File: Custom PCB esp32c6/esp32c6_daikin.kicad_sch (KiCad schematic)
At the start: 31 parts, among them J2 Conn_01x07, Q1 BSS138PS, U1 TPS562246, U2 WT0132C6-S5

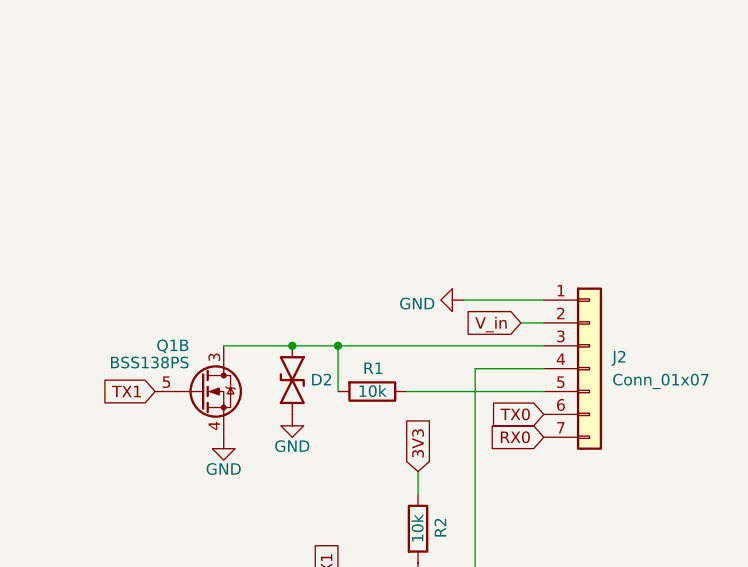
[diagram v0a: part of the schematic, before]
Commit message: fix(sch): add 12V input PTC + TVS and S21 series resistors
TPS562246 is 17V-rec/19V-abs-max on a 12-14V rail with no clamp; SMF15A
clamps hot-plug ring near breakdown, under abs-max. PTC protects the
aircon supply. 220R series resistors cap fault current into the level
shift, per faikin32 baseline BOM.
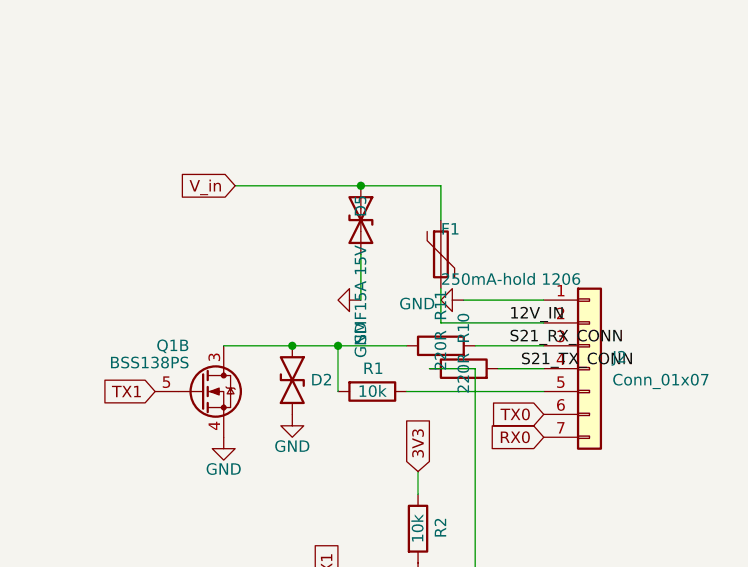
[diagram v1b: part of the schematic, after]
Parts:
- added D5: SMF15A 15V, symbol Device:D_TVS
- added F1: 250mA-hold 1206, symbol Device:Polyfuse
- added R10, R11: 220R, symbol Device:R
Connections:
- net GND: now also D5.2 (A2)
- net V_in: now also D5.1 (A1), F1.1; no longer J2.2 (Pin_2)
- net at D3.2, D4.1 (K), Q1.2 (GN): now also R10.1; no longer J2.4 (Pin_4)
- net at D2.2, Q1.3 (SP), R1.2: now also R11.1; no longer J2.3 (Pin_3)
- new net 12V_IN: F1.2, J2.2 (Pin_2)
- new net S21_RX_CONN: J2.3 (Pin_3), R11.2
- new net S21_TX_CONN: J2.4 (Pin_4), R10.2

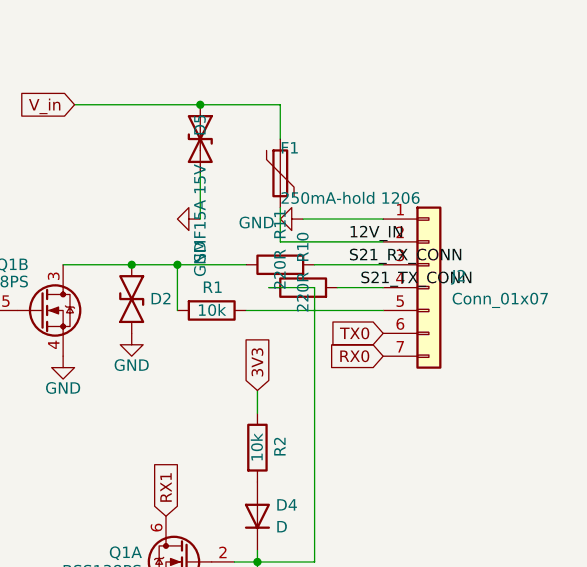
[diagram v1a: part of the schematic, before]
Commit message: feat(sch): S21-standard keyed JST-EH connector
Replaces the non-keyed 7-pin 0.1in header. Standard Daikin BRP069B41
lead mates directly; keying provides the reverse-mate protection.
Debug UART pins dropped; module USB covers debug.
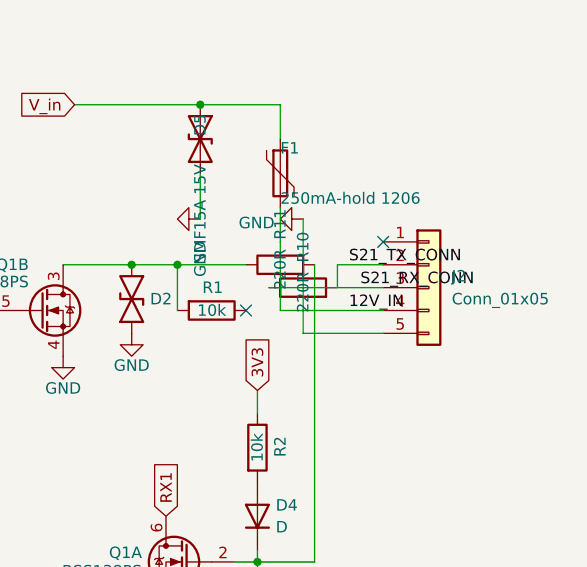
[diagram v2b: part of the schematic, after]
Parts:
- J2: value Conn_01x07 -> Conn_01x05; footprint Connector_PinHeader_2.54mm:PinHeader_1x07_P2.54mm_Horizontal -> Connector_JST:JST_EH_S5B-EH_1x05_P2.50mm_Horizontal; symbol Connector_Generic:Conn_01x07 -> Connector_Generic:Conn_01x05
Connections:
- net 12V_IN: now also J2.4 (Pin_4); no longer J2.2 (Pin_2)
- net GND: now also J2.5 (Pin_5); no longer J2.1 (Pin_1)
- net RX0: no longer J2.7 (Pin_7)
- net S21_RX_CONN: now also D3.2, D4.1 (K), Q1.2 (GN), R10.1
- net S21_TX_CONN: now also J2.2 (Pin_2); no longer J2.4 (Pin_4)
- net TX0: no longer J2.6 (Pin_6)
- net at R1.1: no longer J2.5 (Pin_5)
- no-connect marks 0 -> 2
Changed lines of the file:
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@@
 	(wire
 		(pts
-			(xy 215.9 73.66) (xy 224.79 73.66)
+			(xy 215.9 73.66) (xy 215.9 86.36)
+		)
+		(stroke
+			(width 0)
+			(type default)
+		)
+	)
+	(wire
+		(pts
+			(xy 215.9 86.36) (xy 224.79 86.36)
 		)
 		(stroke
@@
 		)
 	)
-	(wire
-		(pts
-			(xy 209.55 83.82) (xy 224.79 83.82)
-		)
-		(stroke
-			(width 0)
-			(type default)
-		)
+	(no_connect
+		(at 209.55 83.82)
 	)
 	(wire
@@
 	(wire
 		(pts
-			(xy 224.79 76.2) (xy 213.36 76.2)
-		)
-		(stroke
-			(width 0)
-			(type default)
-		)
+			(xy 213.36 76.2) (xy 213.36 83.82)
+		)
+		(stroke
+			(width 0)
+			(type default)
+		)
+	)
+	(wire
+		(pts
+			(xy 213.36 83.82) (xy 224.79 83.82)
+		)
+		(stroke
+			(width 0)
+			(type default)
+		)
+	)
+	(no_connect
+		(at 224.79 76.2)
 	)
 	(wire
@@
 	(wire
 		(pts
-			(xy 219.71 81.28) (xy 224.79 81.28)
+			(xy 219.71 81.28) (xy 219.71 78.74)
+		)
+		(stroke
+			(width 0)
+			(type default)
+		)
+	)
+	(wire
+		(pts
+			(xy 219.71 78.74) (xy 224.79 78.74)
 		)
 		(stroke
@@
 	(wire
 		(pts
-			(xy 217.17 78.74) (xy 224.79 78.74)
+			(xy 217.17 78.74) (xy 217.17 81.28)
+		)
+		(stroke
+			(width 0)
+			(type default)
+		)
+	)
+	(wire
+		(pts
+			(xy 217.17 81.28) (xy 224.79 81.28)
 		)
 		(stroke
@@
 	)
 	(label "12V_IN"
-		(at 220.98 76.2 0)
+		(at 220.98 83.82 0)
 		(effects
 			(font
@@
 	)
 	(label "S21_TX_CONN"
-		(at 222.25 81.28 0)
+		(at 220.98 78.74 0)
 		(effects
 			(font
@@
 	)
 	(label "S21_RX_CONN"
-		(at 220.98 78.74 0)
+		(at 222.25 81.28 0)
 		(effects
 			(font
@@
 		)
 	)
-	(global_label "TX0"
-		(shape input)
-		(at 224.79 86.36 180)
-		(fields_autoplaced yes)
-		(effects
-			(font
-				(size 1.27 1.27)
-			)
-			(justify right)
-		)
-		(property "Intersheetrefs" "${INTERSHEET_REFS}"
-			(at 218.4182 86.36 0)
-			(hide yes)
-			(show_name no)
-			(do_not_autoplace no)
-			(effects
-				(font
-					(size 1.27 1.27)
-				)
-				(justify right)
-			)
-		)
-	)
 	(global_label "3V3"
 		(shape input)
@@
 				)
 				(justify left)
-			)
-		)
-	)
-	(global_label "RX0"
-		(shape input)
-		(at 224.79 88.9 180)
-		(fields_autoplaced yes)
-		(effects
-			(font
-				(size 1.27 1.27)
-			)
-			(justify right)
-		)
-		(property "Intersheetrefs" "${INTERSHEET_REFS}"
-			(at 218.1158 88.9 0)
-			(hide yes)
-			(show_name no)
-			(do_not_autoplace no)
-			(effects
-				(font
-					(size 1.27 1.27)
-				)
-				(justify right)
 			)
 		)
@@
 	)
 	(symbol
-		(lib_id "Connector_Generic:Conn_01x07")
+		(lib_id "Connector_Generic:Conn_01x05")
 		(at 229.87 81.28 0)
 		(unit 1)
@@
 			)
 		)
-		(property "Value" "Conn_01x07"
+		(property "Value" "Conn_01x05"
 			(at 232.41 82.5499 0)
 			(show_name no)
@@
 			)
 		)
-		(property "Footprint" "Connector_PinHeader_2.54mm:PinHeader_1x07_P2.54mm_Horizontal"
+		(property "Footprint" "Connector_JST:JST_EH_S5B-EH_1x05_P2.50mm_Horizontal"
 			(at 229.87 81.28 0)
 			(hide yes)
@@
 			)
 		)
-		(property "Description" "Generic connector, single row, 01x07, script generated (kicad-library-utils/schlib/autogen/connector/)"
+		(property "Description" "Generic connector, single row, 01x05, script generated (kicad-library-utils/schlib/autogen/connector/)"
 			(at 229.87 81.28 0)
 			(hide yes)
@@
 		(pin "5"
 		)
-		(pin "6"
-		)
-		(pin "7"
-		)
 		(instances

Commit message: fix(bom): LCSC part numbers for all placeable parts
U2 and J2 shipped blank and would arrive unplaced from JLC assembly.
New protection parts included. BOM_rev-b.csv is the assembly BOM.
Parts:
- D2, D3: LCSC (none) -> C5137770
- D4: LCSC (none) -> C28642302
- D5: footprint (none) -> Diode_SMD:D_SOD-123F; LCSC (none) -> C123802
- F1: footprint (none) -> Fuse:Fuse_1206_3216Metric; LCSC (none) -> C99561
- J2: LCSC (none) -> C265103
- Q1: LCSC (none) -> C193381
- R1, R2: LCSC (none) -> C25744
- R10, R11: footprint (none) -> Resistor_SMD:R_0603_1608Metric; LCSC (none) -> C1226
- U2: LCSC (none) -> C9900241604
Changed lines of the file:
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@@
 			)
 		)
+		(property "LCSC" "C5137770"
+			(at 210.82 116.205 0)
+			(hide yes)
+			(show_name no)
+			(do_not_autoplace no)
+			(effects
+				(font
+					(size 1.27 1.27)
+				)
+			)
+		)
 		(pin "2"
 		)
@@
 			)
 		)
+		(property "LCSC" "C193381"
+			(at 186.69 83.82 0)
+			(hide yes)
+			(show_name no)
+			(do_not_autoplace no)
+			(effects
+				(font
+					(size 1.27 1.27)
+				)
+			)
+		)
 		(pin "1"
 		)
@@
 			)
 		)
+		(property "LCSC" "C9900241604"
+			(at 88.9 111.76 0)
+			(hide yes)
+			(show_name no)
+			(do_not_autoplace no)
+			(effects
+				(font
+					(size 1.27 1.27)
+				)
+			)
+		)
 		(pin "5"
 		)
@@
 			)
 		)
+		(property "LCSC" "C265103"
+			(at 229.87 81.28 0)
+			(hide yes)
+			(show_name no)
+			(do_not_autoplace no)
+			(effects
+				(font
+					(size 1.27 1.27)
+				)
+			)
+		)
 		(pin "1"
 		)
@@
 			)
 		)
+		(property "LCSC" "C5137770"
+			(at 196.85 82.55 0)
+			(hide yes)
+			(show_name no)
+			(do_not_autoplace no)
+			(effects
+				(font
+					(size 1.27 1.27)
+				)
+			)
+		)
 		(pin "2"
 		)
@@
 			)
 		)
+		(property "LCSC" "C193381"
+			(at 203.2 111.76 0)
+			(hide yes)
+			(show_name no)
+			(do_not_autoplace no)
+			(effects
+				(font
+					(size 1.27 1.27)
+				)
+			)
+		)
 		(pin "1"
 		)
@@
 			)
 		)
+		(property "LCSC" "C28642302"
+			(at 210.82 106.68 0)
+			(hide yes)
+			(show_name no)
+			(do_not_autoplace no)
+			(effects
+				(font
+					(size 1.27 1.27)
+				)
+			)
+		)
 		(pin "1"
 		)
@@
 			)
 		)
+		(property "LCSC" "C25744"
+			(at 205.74 83.82 0)
+			(hide yes)
+			(show_name no)
+			(do_not_autoplace no)
+			(effects
+				(font
+					(size 1.27 1.27)
+				)
+			)
+		)
 		(pin "1"
 		)
@@
 			)
 		)
+		(property "LCSC" "C25744"
+			(at 210.82 99.06 0)
+			(hide yes)
+			(show_name no)
+			(do_not_autoplace no)
+			(effects
+				(font
+					(size 1.27 1.27)
+				)
+			)
+		)
 		(pin "1"
 		)
@@
 			)
 		)
-		(property "Footprint" ""
+		(property "Footprint" "Fuse:Fuse_1206_3216Metric"
 			(at 213.36 68.58 0)
 			(hide yes)
@@
 			)
 		)
+		(property "LCSC" "C99561"
+			(at 213.36 68.58 0)
+			(hide yes)
+			(show_name no)
+			(do_not_autoplace no)
+			(effects
+				(font
+					(size 1.27 1.27)
+				)
+			)
+		)
 		(pin "1"
 		)
@@
 			)
 		)
-		(property "Footprint" ""
+		(property "Footprint" "Diode_SMD:D_SOD-123F"
 			(at 204.47 64.77 0)
 			(hide yes)
@@
 			)
 		)
+		(property "LCSC" "C123802"
+			(at 204.47 64.77 0)
+			(hide yes)
+			(show_name no)
+			(do_not_autoplace no)
+			(effects
+				(font
+					(size 1.27 1.27)
+				)
+			)
+		)
 		(pin "1"
 		)
@@
 			)
 		)
-		(property "Footprint" ""
+		(property "Footprint" "Resistor_SMD:R_0603_1608Metric"
 			(at 215.9 81.28 0)
 			(hide yes)
@@
 			)
 		)
+		(property "LCSC" "C1226"
+			(at 215.9 81.28 0)
+			(hide yes)
+			(show_name no)
+			(do_not_autoplace no)
+			(effects
+				(font
+					(size 1.27 1.27)
+				)
+			)
+		)
 		(pin "1"
 		)
@@
 			)
 		)
-		(property "Footprint" ""
+		(property "Footprint" "Resistor_SMD:R_0603_1608Metric"
 			(at 213.36 78.74 0)
 			(hide yes)
@@
 			(at 213.36 78.74 0)
 			(hide yes)
+			(show_name no)
+			(do_not_autoplace no)
+			(effects
+				(font
+					(size 1.27 1.27)
+				)
+			)
+		)
+		(property "LCSC" "C1226"
+			(at 213.36 78.74 0)
+			(hide yes)

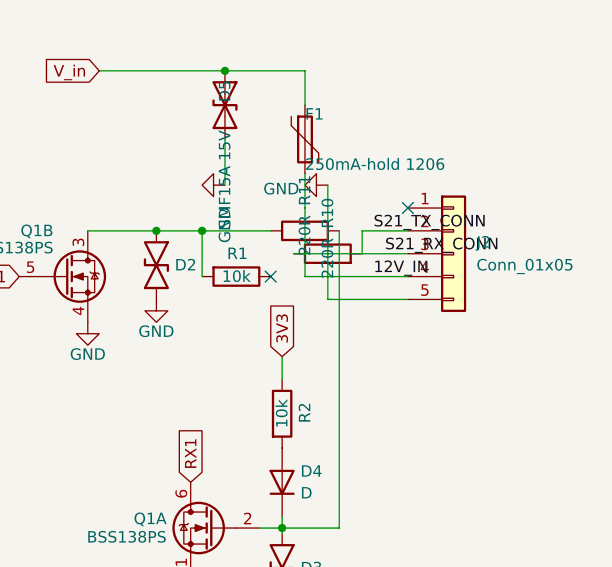
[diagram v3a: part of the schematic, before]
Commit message: fix(sch+pcb): separate the two S21 signal nets merged by the JST-EH swap
The Task-6 JST-EH connector swap merged two S21 nets into one, tying
J2 pin 2 (aircon Tx) and J2 pin 3 (aircon Rx) together through R10 (220R)
and feeding the ESP's TX back into its RX front end. A single wire carrying
the /S21_RX_CONN label at the R10.1 row shorted J2.3, R11.2, and the
Q1.2/D3/D4 gate cluster onto one 6-node net.

This restores the Task-5 (commit 2981aef) two-net split, adapted to the new
JST-EH pin numbers:
  - /S21_TX_CORE (new label; was Net-(D4-K)) = {R10.1, Q1.2, D3.2, D4.1}
  - /S21_RX_CONN (reduced to)                = {J2.3, R11.2}
J2.2 and J2.3 now share no path except through the intended full front end.

Schematic: split the merge wire into two electrically separate wires and
added the S21_TX_CORE label; the four nets are netlist-verified (kicad-cli
export) with exactly the target node sets. ERC unchanged at 16 errors.

PCB: created net /S21_TX_CORE, reassigned pads R10.1/Q1.2/D3.2/D4.1 and
their cluster copper to it, deleted the two bridge tracks (R11.2->R10.1
vertical on F.Cu and J2.3->hub on B.Cu), and routed a new R11.2->J2.3 RX
path (F.Cu stub + via + B.Cu run under the 12V/TX columns). DRC clean:
0 unconnected, 0 errors, 0 schematic-parity mismatches, 1 zone.

refill.py: corrected the wx assert-suppression guard order (DisableAsserts
after importing pcbnew, with a wx.App) so refills no longer raise dialogs.
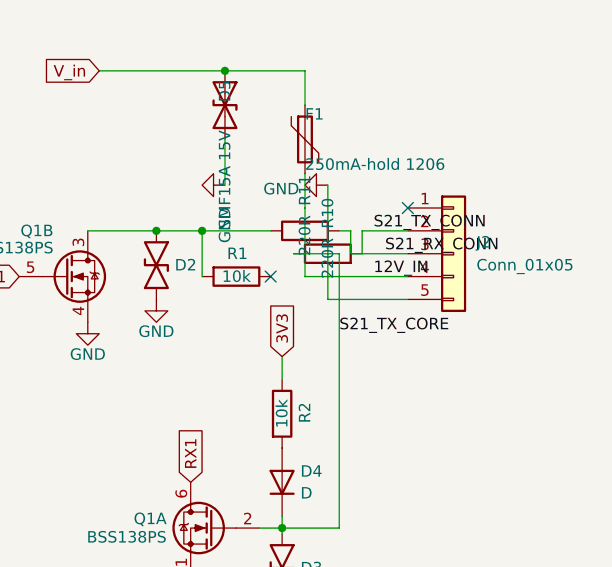
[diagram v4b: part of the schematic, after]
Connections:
- net S21_RX_CONN: no longer D3.2, D4.1 (K), Q1.2 (GN), R10.1
- new net S21_TX_CORE: D3.2, D4.1 (K), Q1.2 (GN), R10.1
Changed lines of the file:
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@@
 	(wire
 		(pts
-			(xy 217.17 78.74) (xy 217.17 81.28)
+			(xy 217.17 78.74) (xy 218.44 78.74)
 		)
 		(stroke
@@
 	(wire
 		(pts
-			(xy 217.17 81.28) (xy 224.79 81.28)
+			(xy 218.44 81.28) (xy 224.79 81.28)
 		)
 		(stroke
@@
 		(effects
 			(font
+				(size 1.27 1.27)
+			)
+			(justify left bottom)
+		)
+	)
+	(wire
+		(pts
+			(xy 218.44 78.74) (xy 218.44 81.28)
+		)
+		(stroke
+			(width 0)
+			(type default)
+		)
+	)
+	(label "S21_TX_CORE"
+		(at 217.17 90.17 0)
+		(effects
+			(font

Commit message: feat(xiao-sch): delete WT0132C6 module + button circuitry
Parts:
- removed Boot1, Matter1, Reset1: Tactile Button, 160gf, easyeda2kicad:SW-SMD_L3.9-W3.0-P4.45, symbol JLCPCB-Connectors_Buttons:Tactile Button, 160gf, 12V, 50mA, 4.0mm
- removed C1, C2, C4, C5, C7, C8: 100nF, easyeda2kicad:C0402, symbol Device:C
- removed C6: 1uF, easyeda2kicad:C0603, symbol Device:C
- removed D4: D, easyeda2kicad:D0402, symbol Device:D
- removed R9: 220, easyeda2kicad:R0402, symbol Device:R
- removed U2: WT0132C6-S5, easyeda2kicad:WT0132C6-S5, symbol easyeda2kicad:WT0132C6-S5

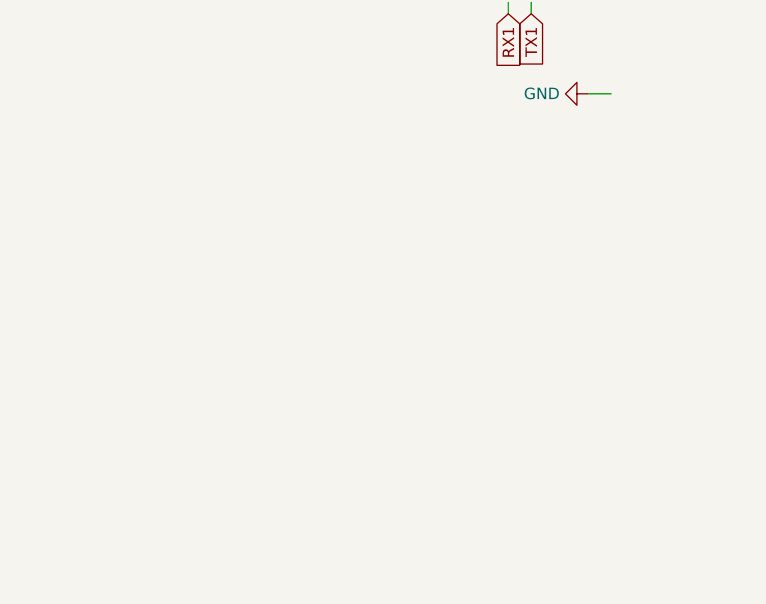
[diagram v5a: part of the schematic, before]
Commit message: feat(xiao-sch): add XIAO ESP32-C6 symbol + both-capable footprint
Add U2 = Seeed XIAO ESP32-C6, reusing the reference designator freed
by the Task 2 module deletion. Not wired yet (Tasks 4/5 wire UART and
power); pins left ready.

Source: official Seeed OPL KiCad library (Seeed-Studio/OPL_Kicad_Library,
"Seeed Studio XIAO Series Library"). Symbol XIAO-ESP32-C6-SMD (24 pins)
and footprint XIAO-ESP32-C6-DIP copied verbatim into a project-local lib
(lib/Seeed_Studio_XIAO_Series.kicad_sym, lib/Seeed_XIAO.pretty) with new
sym-lib-table / fp-lib-table.

Footprint is both-capable by construction: each of the 14 main edge pads
has BOTH a plated through-hole (header/socket mount) and an outward SMD
edge pad (direct edge-reflow). 2 rows of 7, 2.54mm pitch, 15.24mm
row-to-row spacing per the Seeed mechanical drawing. Default footprint
of the project symbol set to the DIP (both-capable) variant.

Named pads verified against the official pinout: D6=pad7 (GPIO16/TX),
D7=pad8 (GPIO17/RX), 3V3_OUT=pad12, GND=pad13, VBUS=pad14 (5V pad).
Symbol pins 1-14 map 1:1 to footprint pads 1-14. Symbol pins 15-24 are
the module's optional bottom debug (JTAG/EN/BOOT) and battery (VBAT/GND)
pads, all passive and unused here; a DIP/header land pattern cannot land
them (not on the edge), so they are intentionally unconnected.

Verify: netlist exports clean, U2 present; ERC delta vs Task 2 is only
+24 pin_not_connected (U2's unwired pins), no other new violations.
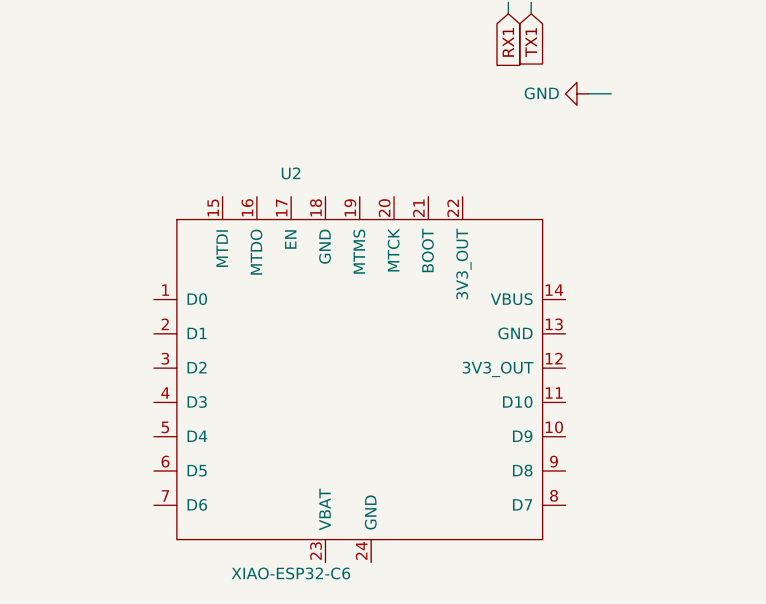
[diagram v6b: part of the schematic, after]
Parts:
- added U2: XIAO-ESP32-C6, Seeed_XIAO:XIAO-ESP32-C6-DIP, symbol Seeed_Studio_XIAO_Series:XIAO-ESP32-C6-SMD
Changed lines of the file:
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@@
+		)
+	)
+	(symbol
+		(lib_id "Seeed_Studio_XIAO_Series:XIAO-ESP32-C6-SMD")
+		(at 63.5 170.18 0)
+		(unit 1)
+		(body_style 1)
+		(exclude_from_sim no)
+		(in_bom yes)
+		(on_board yes)
+		(in_pos_files yes)
+		(dnp no)
+		(property "Reference" "U2"
+			(at 63.5 148.59 0)
+			(effects
+				(font
+					(size 1.27 1.27)
+				)
+			)
+		)
+		(property "Value" "XIAO-ESP32-C6"
+			(at 63.5 193.04 0)
+			(effects
+				(font
+					(size 1.27 1.27)
+				)
+			)
+		)
+		(property "Footprint" "Seeed_XIAO:XIAO-ESP32-C6-DIP"
+			(at 63.5 170.18 0)
+			(hide yes)
+			(effects
+				(font
+					(size 1.27 1.27)
+				)
+			)
+		)
+		(property "Datasheet" "https://wiki.seeedstudio.com/xiao_esp32c6_getting_started/"
+			(at 63.5 170.18 0)
+			(hide yes)
+			(effects
+				(font
+					(size 1.27 1.27)
+				)
+			)
+		)
+		(property "Description" "Seeed Studio XIAO ESP32-C6"
+			(at 63.5 170.18 0)
+			(hide yes)
+			(effects
+				(font
+					(size 1.27 1.27)
+				)
+			)
+		)
+		(pin "1"
+		)
+		(pin "2"
+		)
+		(pin "3"
+		)
+		(pin "4"
+		)
+		(pin "5"
+		)
+		(pin "6"
+		)
+		(pin "7"
+		)
+		(pin "8"
+		)
+		(pin "9"
+		)
+		(pin "10"
+		)
+		(pin "11"
+		)
+		(pin "12"
+		)
+		(pin "13"
+		)
+		(pin "14"
+		)
+		(pin "15"
+		)
+		(pin "16"
+		)
+		(pin "17"
+		)
+		(pin "18"
+		)
+		(pin "19"
+		)
+		(pin "20"
+		)
+		(pin "21"
+		)
+		(pin "22"
+		)
+		(pin "23"
+		)
+		(pin "24"
+		)
+		(instances
+			(project "esp32c6_daikin"
+				(path "/46c350bb-7de4-4e81-aafd-4af55e37aab0"
+					(reference "U2")
+					(unit 1)
+				)
+			)
 		)
 	)
